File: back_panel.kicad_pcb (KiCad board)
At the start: 2 copper layers, 300 x 105 mm, 121 parts

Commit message: more manual updating before sending to print
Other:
- outline, holes or cut-outs redrawn
- board text added: "880 back panel r1.2 11/2018"
- board text removed: "880 back panel r1.1 11/2018"
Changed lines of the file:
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@@
     (35 F.Paste user)
     (36 B.SilkS user)
-    (37 F.SilkS user hide)
+    (37 F.SilkS user)
     (38 B.Mask user)
     (39 F.Mask user)
@@
     (mod_text_size 1 1)
     (mod_text_width 0.15)
-    (pad_size 2.75 2.75)
-    (pad_drill 0)
+    (pad_size 5.5 5.5)
+    (pad_drill 5.5)
     (pad_to_mask_clearance 0)
     (aux_axis_origin 0 0)
@@
       (effects (font (size 1.5 1.5) (thickness 0.15)))
     )
-    (pad "" np_thru_hole circle (at 5.35 0.35) (size 5 5) (drill 5) (layers *.Cu *.Mask F.SilkS))
+    (pad "" np_thru_hole circle (at 5.35 0.35) (size 5.5 5.5) (drill 5.5) (layers *.Cu *.Mask F.SilkS))
   )
   (module MyModules:SNAP_HOLE_0.125_INCH (layer F.Cu)
@@
       (effects (font (size 1.5 1.5) (thickness 0.15)))
     )
-    (pad "" np_thru_hole circle (at 5.35 0.35) (size 5 5) (drill 5) (layers *.Cu *.Mask F.SilkS))
+    (pad "" np_thru_hole circle (at 5.35 0.35) (size 5.5 5.5) (drill 5.5) (layers *.Cu *.Mask F.SilkS))
   )
   (module MyModules:SNAP_HOLE_0.125_INCH (layer F.Cu)
@@
     (effects (font (size 1.5 1.5) (thickness 0.3)) (justify mirror))
   )
-  (gr_text "1.25 ms" (at 277.5 121.65) (layer B.Cu)
+  (gr_text "1.25 ms" (at 277.5 121.15) (layer B.Cu)
     (effects (font (size 1.5 1.5) (thickness 0.3)) (justify mirror))
   )
@@
     (effects (font (size 1.5 1.5) (thickness 0.3)) (justify mirror))
   )
-  (gr_text NOISE (at 212.3 130.25) (layer B.Cu)
+  (gr_text NOISE (at 212.3 130.5) (layer B.Cu)
     (effects (font (size 1.5 1.5) (thickness 0.3)) (justify mirror))
   )
@@
   (gr_line (start 114.15 77.75) (end 106.15 77.75) (layer Edge.Cuts) (width 0.2))
   (gr_line (start 106.15 77.75) (end 106.15 66.15) (layer Edge.Cuts) (width 0.2))
-  (gr_text "880 back panel r1.1 11/2018" (at 192.2 152.95) (layer F.SilkS)
+  (gr_text "880 back panel r1.2 11/2018" (at 192.2 152.95) (layer F.SilkS)
     (effects (font (size 1.5 1.5) (thickness 0.3)))
   )
@@
     (effects (font (size 1.5 1.5) (thickness 0.3)) (justify mirror))
   )
-  (gr_line (start 215.2 123.25) (end 213.6 123.95) (layer B.Cu) (width 0.35))
-  (gr_line (start 213.6 123.95) (end 213.3 122.25) (layer B.Cu) (width 0.35))
-  (gr_line (start 218 116.05) (end 213.6 123.95) (layer B.Cu) (width 0.35))
-  (gr_line (start 215.2 123.25) (end 213.6 123.95) (layer B.Mask) (width 0.35))
-  (gr_line (start 213.6 123.95) (end 213.3 122.25) (layer B.Mask) (width 0.35))
-  (gr_line (start 218 116.05) (end 213.6 123.95) (layer B.Mask) (width 0.35))
-  (gr_text NOISE (at 212.3 130.25) (layer B.Mask)
+  (gr_line (start 215.3 122.95) (end 213.7 123.65) (layer B.Cu) (width 0.35))
+  (gr_line (start 213.7 123.65) (end 213.4 121.95) (layer B.Cu) (width 0.35))
+  (gr_line (start 216.75 118.17) (end 213.7 123.65) (layer B.Cu) (width 0.35))
+  (gr_line (start 215.3 122.95) (end 213.7 123.65) (layer B.Mask) (width 0.35))
+  (gr_line (start 213.7 123.65) (end 213.4 121.95) (layer B.Mask) (width 0.35))
+  (gr_line (start 216.76 118.15) (end 213.7 123.65) (layer B.Mask) (width 0.35))
+  (gr_text NOISE (at 212.3 130.5) (layer B.Mask)
     (effects (font (size 1.5 1.5) (thickness 0.3)) (justify mirror))
   )
@@
     (effects (font (size 1.5 1.5) (thickness 0.3)) (justify mirror))
   )
-  (gr_line (start 275 126.55) (end 274.2 127.75) (layer B.Cu) (width 0.35))
-  (gr_line (start 275 126.55) (end 273.6 126.15) (layer B.Cu) (width 0.35))
-  (gr_line (start 272.4 127.45) (end 275 126.55) (layer B.Cu) (width 0.35))
-  (gr_line (start 275 126.55) (end 274.2 127.75) (layer B.Mask) (width 0.35))
-  (gr_line (start 275 126.55) (end 273.6 126.15) (layer B.Mask) (width 0.35))
-  (gr_line (start 272.4 127.45) (end 275 126.55) (layer B.Mask) (width 0.35))
+  (gr_line (start 274.64 126.51) (end 273.84 127.71) (layer B.Cu) (width 0.35))
+  (gr_line (start 274.64 126.51) (end 273.24 126.11) (layer B.Cu) (width 0.35))
+  (gr_line (start 272.04 127.41) (end 274.64 126.51) (layer B.Cu) (width 0.35))
+  (gr_line (start 274.64 126.51) (end 273.84 127.71) (layer B.Mask) (width 0.35))
+  (gr_line (start 274.64 126.51) (end 273.24 126.11) (layer B.Mask) (width 0.35))
+  (gr_line (start 272.04 127.41) (end 274.64 126.51) (layer B.Mask) (width 0.35))
   (gr_text "1.85 ms" (at 292.4 107.4) (layer B.Mask)
     (effects (font (size 1.5 1.5) (thickness 0.3)) (justify mirror))
@@
     (effects (font (size 1.5 1.5) (thickness 0.3)) (justify mirror))
   )
-  (gr_text "1.25 ms" (at 277.5 121.65) (layer B.Mask)
+  (gr_text "1.25 ms" (at 277.5 121.15) (layer B.Mask)
     (effects (font (size 1.5 1.5) (thickness 0.3)) (justify mirror))
   )
@@
   (gr_line (start 70.575 91.4) (end 70.575 98.125) (angle 90) (layer Edge.Cuts) (width 0.2))
   (gr_line (start 70.575 91.4) (end 76.975 91.4) (angle 90) (layer Edge.Cuts) (width 0.2))
-  (gr_line (start 91.4 96.15) (end 82.15 96.15) (angle 90) (layer Edge.Cuts) (width 0.2))
-  (gr_line (start 91.4 108.9) (end 91.4 96.15) (angle 90) (layer Edge.Cuts) (width 0.2))
-  (gr_line (start 82.15 108.9) (end 91.4 108.9) (angle 90) (layer Edge.Cuts) (width 0.2))
-  (gr_line (start 82.15 96.15) (end 82.15 108.9) (angle 90) (layer Edge.Cuts) (width 0.2))
+  (gr_line (start 91.65 96.15) (end 82.65 96.15) (angle 90) (layer Edge.Cuts) (width 0.2))
+  (gr_line (start 91.65 108.9) (end 91.65 96.15) (angle 90) (layer Edge.Cuts) (width 0.2))
+  (gr_line (start 82.65 108.9) (end 91.65 108.9) (angle 90) (layer Edge.Cuts) (width 0.2))
+  (gr_line (start 82.65 96.15) (end 82.65 108.9) (angle 90) (layer Edge.Cuts) (width 0.2))
   (gr_line (start 162.65 140.4) (end 162.65 129.9) (angle 90) (layer Edge.Cuts) (width 0.2))
   (gr_line (start 197.15 140.4) (end 162.65 140.4) (angle 90) (layer Edge.Cuts) (width 0.2))

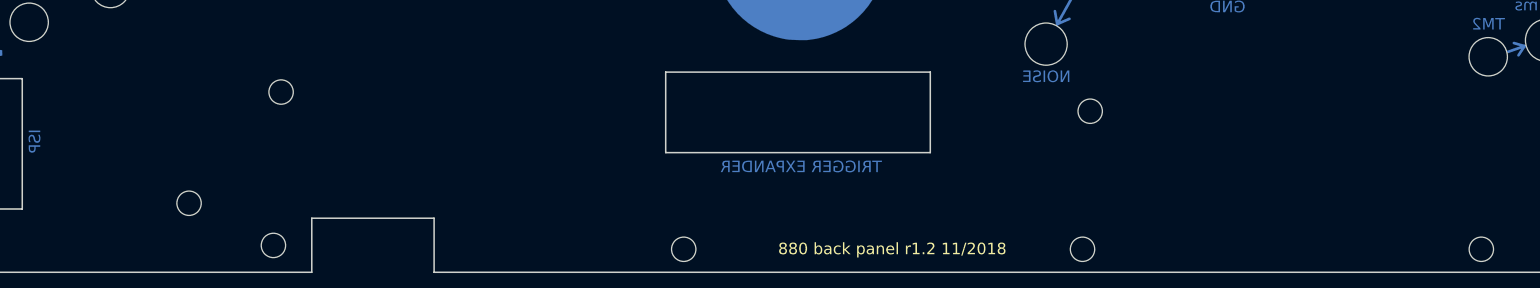
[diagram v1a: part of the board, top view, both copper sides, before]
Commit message: changes to back panel for B series run
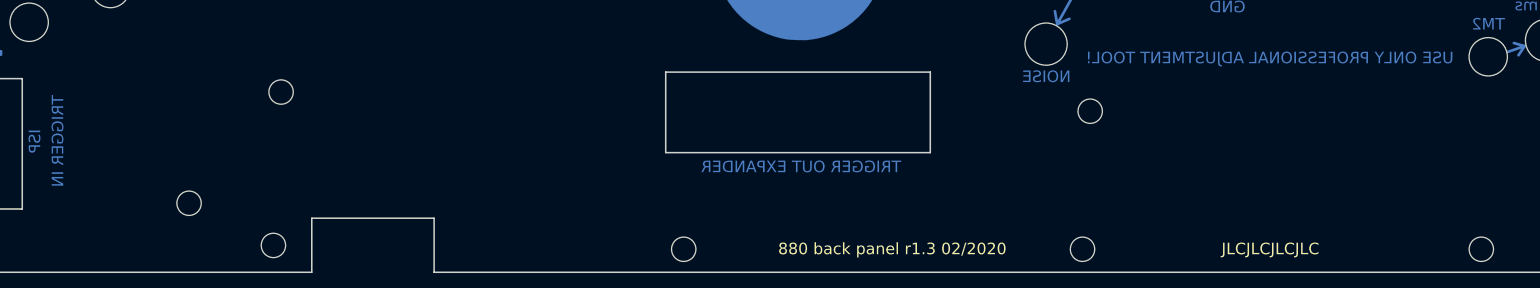
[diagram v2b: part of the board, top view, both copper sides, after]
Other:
- board text added: "880 back panel r1.3 02/2020"
- board text added: "JLCJLCJLCJLC"
- board text added: "TRIGGER IN"
- board text added: "TRIGGER OUT EXPANDER"
- board text added: "USE ONLY PROFESSIONAL ADJUSTMENT TOOL!"
- board text removed: "880 back panel r1.2 11/2018"
- board text removed: "TRIGGER EXPANDER"
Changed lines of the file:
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@@
     (area 67.899999 50.899999 368.100001 156.100001)
     (thickness 1.6)
-    (drawings 443)
+    (drawings 448)
     (tracks 79)
     (zones 0)
@@
       (clearance 1))
   )
+  (gr_text "TRIGGER IN" (at 83.4 138.9 90) (layer B.Cu)
+    (effects (font (size 1.5 1.5) (thickness 0.3)) (justify mirror))
+  )
+  (gr_text "TRIGGER IN" (at 83.4 138.9 90) (layer B.Mask)
+    (effects (font (size 1.5 1.5) (thickness 0.3)) (justify mirror))
+  )
+  (gr_text "USE ONLY PROFESSIONAL ADJUSTMENT TOOL!" (at 241.4 128.05) (layer B.Mask)
+    (effects (font (size 1.5 1.5) (thickness 0.3)) (justify mirror))
+  )
+  (gr_text "USE ONLY PROFESSIONAL ADJUSTMENT TOOL!" (at 241.4 128.05) (layer B.Cu)
+    (effects (font (size 1.5 1.5) (thickness 0.3)) (justify mirror))
+  )
+  (gr_text JLCJLCJLCJLC (at 241.5 152.95) (layer F.SilkS)
+    (effects (font (size 1.5 1.5) (thickness 0.3)))
+  )
   (gr_arc (start 77.1 98.35) (end 68.1 81.05) (angle 234.3) (layer B.Cu) (width 1))
   (gr_arc (start 77.1 98.35) (end 68.1 81.05) (angle 234.3) (layer B.Mask) (width 1))
@@
     (effects (font (size 1.5 1.5) (thickness 0.3)) (justify mirror))
   )
-  (gr_text "TRIGGER EXPANDER" (at 180.3 142.25) (layer B.Cu)
+  (gr_text "TRIGGER OUT EXPANDER" (at 180.3 142.25) (layer B.Cu)
     (effects (font (size 1.5 1.5) (thickness 0.3)) (justify mirror))
   )
@@
   (gr_line (start 114.15 77.75) (end 106.15 77.75) (layer Edge.Cuts) (width 0.2))
   (gr_line (start 106.15 77.75) (end 106.15 66.15) (layer Edge.Cuts) (width 0.2))
-  (gr_text "880 back panel r1.2 11/2018" (at 192.2 152.95) (layer F.SilkS)
+  (gr_text "880 back panel r1.3 02/2020" (at 192.2 152.95) (layer F.SilkS)
     (effects (font (size 1.5 1.5) (thickness 0.3)))
   )
@@
     (effects (font (size 1.5 1.5) (thickness 0.3)) (justify mirror))
   )
-  (gr_text "TRIGGER EXPANDER" (at 180.3 142.25) (layer B.Mask)
+  (gr_text "TRIGGER OUT EXPANDER" (at 180.3 142.25) (layer B.Mask)
     (effects (font (size 1.5 1.5) (thickness 0.3)) (justify mirror))
   )
